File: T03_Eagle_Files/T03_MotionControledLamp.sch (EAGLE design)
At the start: 32 parts, among them U1 ATMEGA328P-MU, U4 TPS61161ADRVT, X2 16MHz

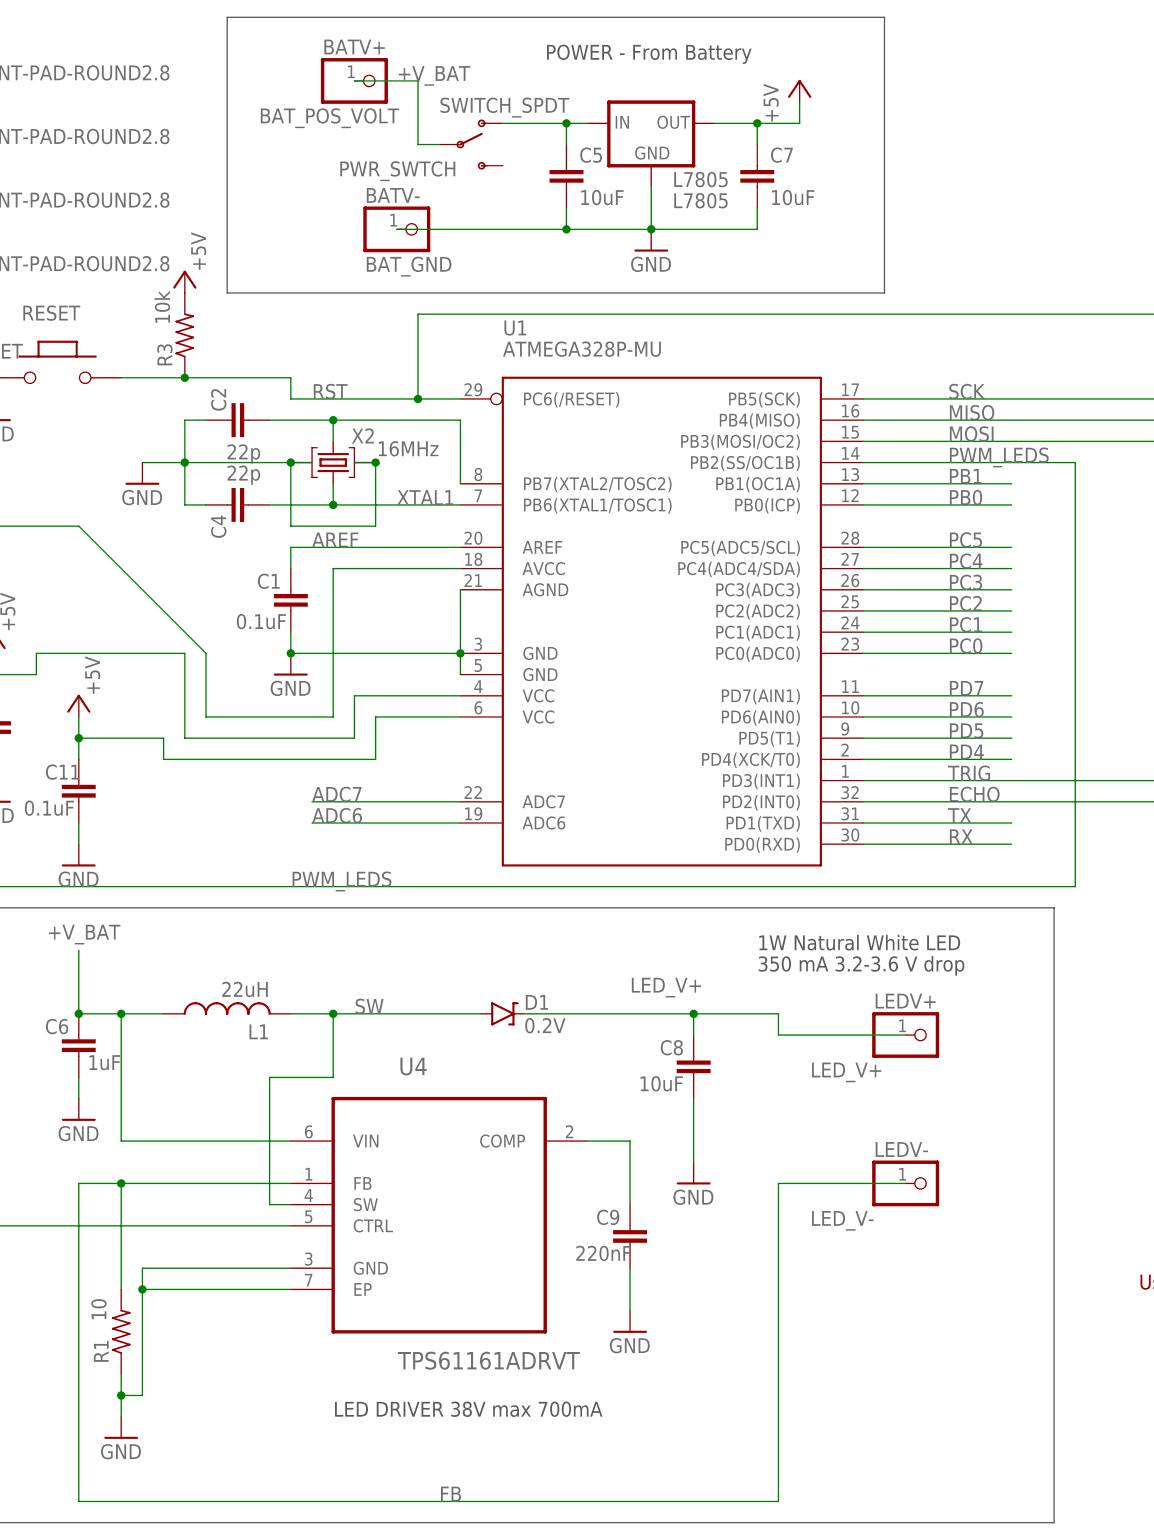
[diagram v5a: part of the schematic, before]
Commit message: Added molex headers to schematic
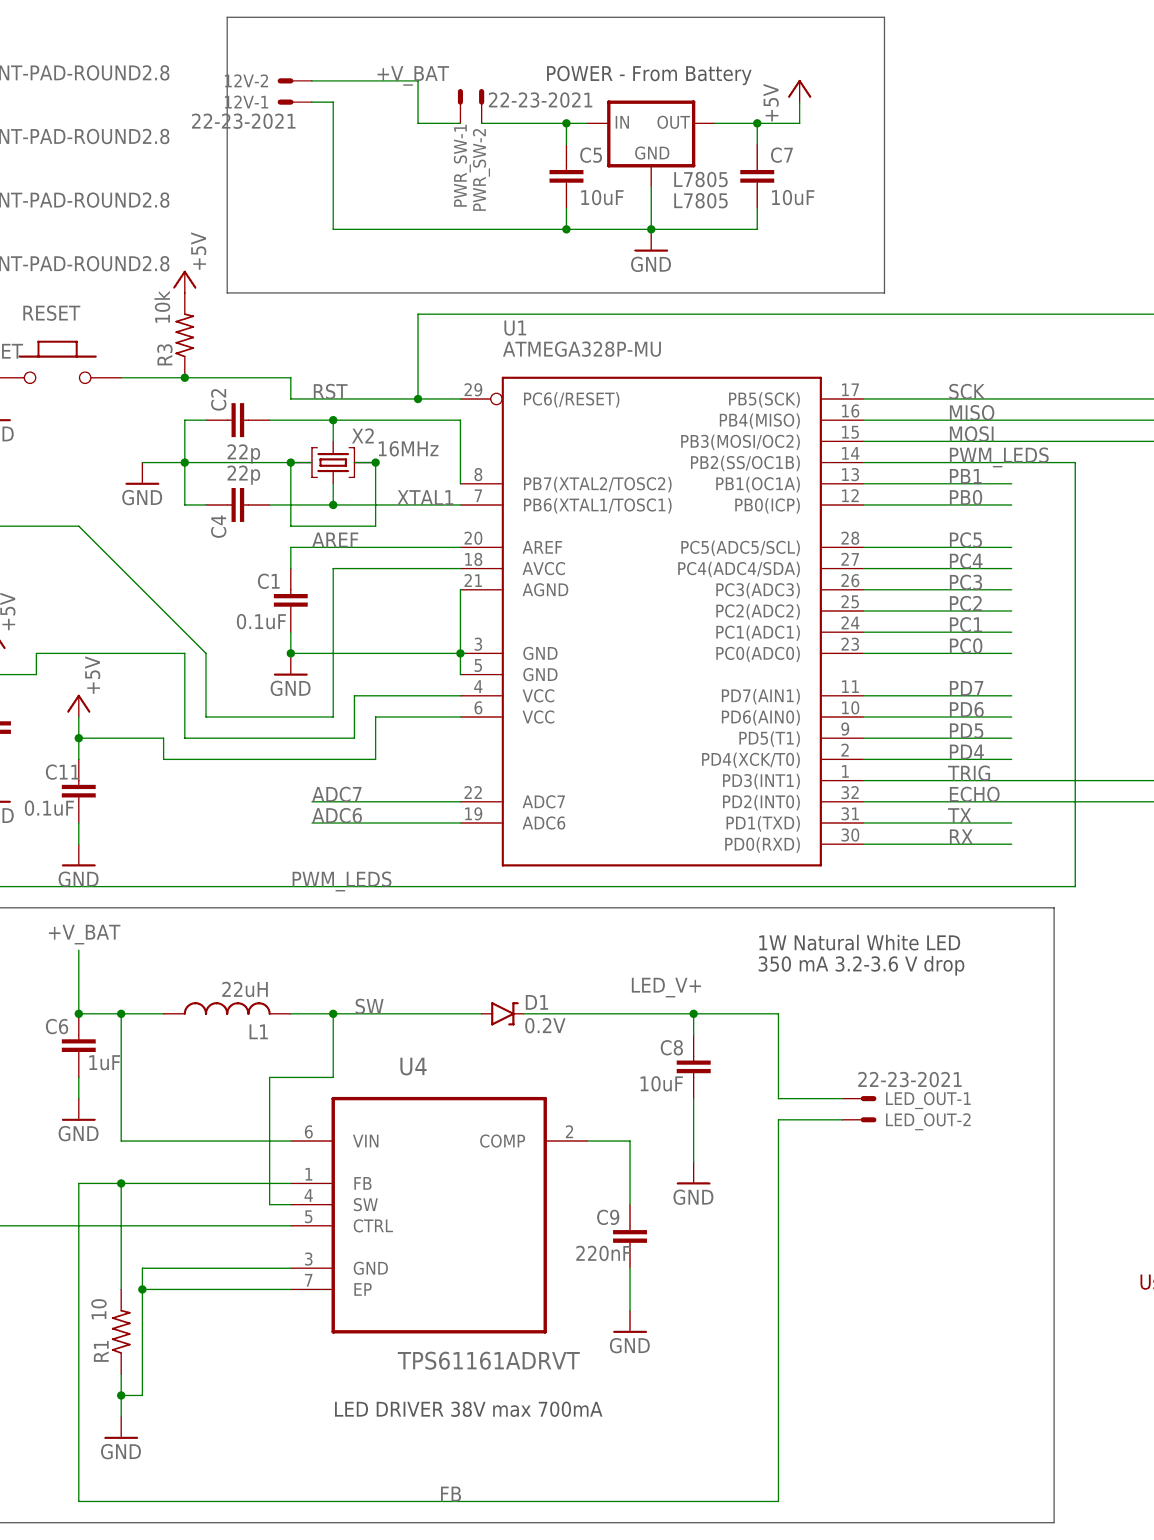
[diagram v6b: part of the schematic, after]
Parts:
- removed BATV+: BAT_POS_VOLT, adafruit:PINHD-1X1
- removed BATV-: BAT_GND, adafruit:PINHD-1X1
- removed LEDV+: LED_V+, adafruit:PINHD-1X1
- removed LEDV-: LED_V-, adafruit:PINHD-1X1
- removed PWR_SWTCH: SWITCH_SPDT, SparkFun-Electromechanical:SWITCH_SPDT
- added 12V, LED_OUT, PWR_SW: 22-23-2021, con-molex:22-23-2021
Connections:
- net +V_BAT: now also 12V-2.S, PWR_SW-1.S; no longer BATV+.1, PWR_SWTCH.P
- net FB: now also LED_OUT-2.S; no longer LEDV-.1
- net GND: now also 12V-1.S; no longer BATV-.1
- net LED_V+: now also LED_OUT-1.S; no longer LEDV+.1
- net N$4: now also PWR_SW-2.S; no longer PWR_SWTCH.O
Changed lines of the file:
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@@
 <part name="C5" library="rcl" deviceset="C-EU" device="C1206" value="10uF"/>
 <part name="C7" library="rcl" deviceset="C-EU" device="C1206" value="10uF"/>
-<part name="PWR_SWTCH" library="SparkFun-Electromechanical" deviceset="SWITCH_SPDT" device=""/>
 <part name="JP1" library="SparkFun-Connectors" deviceset="M05X2" device="SHD_LOCK" value="AVR_SPI_PROG"/>
 <part name="GND6" library="SparkFun-Aesthetics" deviceset="GND" device=""/>
@@
 <part name="GND10" library="supply1" deviceset="GND" device=""/>
 <part name="GND11" library="supply1" deviceset="GND" device=""/>
-<part name="BATV+" library="adafruit" deviceset="PINHD-1X1" device="" value="BAT_POS_VOLT"/>
-<part name="BATV-" library="adafruit" deviceset="PINHD-1X1" device="" value="BAT_GND"/>
 <part name="R3" library="rcl" deviceset="R-US_" device="M1206" value="10k"/>
 <part name="L7805" library="v-reg" deviceset="78XXL" device="" value="L7805"/>
 <part name="SR04" library="con-molex" deviceset="22-23-2041" device=""/>
-<part name="LEDV+" library="adafruit" deviceset="PINHD-1X1" device="" value="LED_V+"/>
-<part name="LEDV-" library="adafruit" deviceset="PINHD-1X1" device="" value="LED_V-"/>
 <part name="P+5" library="supply1" deviceset="+5V" device=""/>
 <part name="H1" library="holes" deviceset="MOUNT-PAD-ROUND" device="2.8"/>
@@
 <part name="P+9" library="supply1" deviceset="+5V" device=""/>
 <part name="GND14" library="SparkFun-Aesthetics" deviceset="GND" device=""/>
+<part name="PWR_SW" library="con-molex" deviceset="22-23-2021" device=""/>
+<part name="12V" library="con-molex" deviceset="22-23-2021" device=""/>
+<part name="LED_OUT" library="con-molex" deviceset="22-23-2021" device=""/>
 </parts>
 <sheets>
@@
 <wire x1="43.18" y1="149.86" x2="121.92" y2="149.86" width="0.1524" layer="97"/>
 <wire x1="121.92" y1="149.86" x2="121.92" y2="182.88" width="0.1524" layer="97"/>
-<text x="81.28" y="177.8" size="1.778" layer="97">POWER - From Battery</text>
+<text x="81.28" y="175.26" size="1.778" layer="97">POWER - From Battery</text>
 <wire x1="167.64" y1="119.38" x2="167.64" y2="68.58" width="0.1524" layer="97"/>
 <wire x1="167.64" y1="68.58" x2="238.76" y2="68.58" width="0.1524" layer="97"/>
@@
 <instance part="C5" gate="G$1" x="83.82" y="165.1"/>
 <instance part="C7" gate="G$1" x="106.68" y="165.1"/>
-<instance part="PWR_SWTCH" gate="G$1" x="71.12" y="167.64" smashed="yes">
-<attribute name="NAME" x="56.515" y="163.83" size="1.778" layer="95"/>
-<attribute name="VALUE" x="68.58" y="171.45" size="1.778" layer="96"/>
-</instance>
 <instance part="JP1" gate="G$1" x="208.28" y="162.56"/>
 <instance part="GND6" gate="1" x="228.6" y="149.86"/>
@@
 <instance part="GND10" gate="1" x="25.4" y="50.8"/>
 <instance part="GND11" gate="1" x="91.44" y="25.4"/>
-<instance part="BATV+" gate="G$1" x="60.96" y="175.26" smashed="yes">
-<attribute name="NAME" x="54.61" y="178.435" size="1.778" layer="95"/>
-<attribute name="VALUE" x="46.99" y="170.18" size="1.778" layer="96"/>
-</instance>
-<instance part="BATV-" gate="G$1" x="66.04" y="157.48" smashed="yes">
-<attribute name="NAME" x="59.69" y="160.655" size="1.778" layer="95"/>
-<attribute name="VALUE" x="59.69" y="152.4" size="1.778" layer="96"/>
-</instance>
 <instance part="R3" gate="G$1" x="38.1" y="144.78" smashed="yes" rot="R90">
 <attribute name="NAME" x="36.6014" y="140.97" size="1.778" layer="95" rot="R90"/>
@@
 <instance part="SR04" gate="-3" x="190.5" y="93.98"/>
 <instance part="SR04" gate="-4" x="190.5" y="91.44"/>
-<instance part="LEDV+" gate="G$1" x="127" y="60.96" smashed="yes">
-<attribute name="NAME" x="120.65" y="64.135" size="1.778" layer="95"/>
-<attribute name="VALUE" x="113.03" y="55.88" size="1.778" layer="96"/>
-</instance>
-<instance part="LEDV-" gate="G$1" x="127" y="43.18" smashed="yes">
-<attribute name="NAME" x="120.65" y="46.355" size="1.778" layer="95"/>
-<attribute name="VALUE" x="113.03" y="38.1" size="1.778" layer="96"/>
-</instance>
 <instance part="P+5" gate="1" x="38.1" y="152.4" smashed="yes">
 <attribute name="VALUE" x="40.64" y="152.4" size="1.778" layer="96" rot="R90"/>
@@
 </instance>
 <instance part="GND14" gate="1" x="228.6" y="91.44"/>
+<instance part="PWR_SW" gate="-1" x="71.12" y="172.72" smashed="yes" rot="R90">
+<attribute name="NAME" x="70.358" y="170.18" size="1.524" layer="95" rot="R270"/>
+<attribute name="VALUE" x="87.122" y="173.863" size="1.778" layer="96" rot="R180"/>
+</instance>
+<instance part="PWR_SW" gate="-2" x="73.66" y="172.72" smashed="yes" rot="R90">
+<attribute name="NAME" x="74.168" y="159.512" size="1.524" layer="95" rot="R90"/>
+</instance>
+<instance part="12V" gate="-1" x="50.8" y="172.72" rot="R180"/>
+<instance part="12V" gate="-2" x="50.8" y="175.26" rot="R180"/>
+<instance part="LED_OUT" gate="-1" x="119.38" y="53.34"/>
+<instance part="LED_OUT" gate="-2" x="119.38" y="50.8"/>
 </instances>
 <busses>
@@
 <wire x1="83.82" y1="157.48" x2="93.98" y2="157.48" width="0.1524" layer="91"/>
 <junction x="83.82" y="157.48"/>
-<pinref part="BATV-" gate="G$1" pin="1"/>
-<wire x1="83.82" y1="157.48" x2="63.5" y2="157.48" width="0.1524" layer="91"/>
+<wire x1="83.82" y1="157.48" x2="55.88" y2="157.48" width="0.1524" layer="91"/>
 <pinref part="L7805" gate="A" pin="GND"/>
+<wire x1="55.88" y1="157.48" x2="55.88" y2="172.72" width="0.1524" layer="91"/>
+<pinref part="12V" gate="-1" pin="S"/>
+<wire x1="55.88" y1="172.72" x2="53.34" y2="172.72" width="0.1524" layer="91"/>
 </segment>
 <segment>
@@
 <pinref part="C5" gate="G$1" pin="1"/>
 <wire x1="83.82" y1="170.18" x2="83.82" y2="167.64" width="0.1524" layer="91"/>
-<pinref part="PWR_SWTCH" gate="G$1" pin="O"/>
-<wire x1="76.2" y1="170.18" x2="83.82" y2="170.18" width="0.1524" layer="91"/>
+<wire x1="73.66" y1="170.18" x2="83.82" y2="170.18" width="0.1524" layer="91"/>
 <junction x="83.82" y="170.18"/>
 <pinref part="L7805" gate="A" pin="IN"/>
+<pinref part="PWR_SW" gate="-2" pin="S"/>
 </segment>
 </net>
@@
 <wire x1="78.74" y1="63.5" x2="99.06" y2="63.5" width="0.1524" layer="91"/>
 <wire x1="99.06" y1="63.5" x2="109.22" y2="63.5" width="0.1524" layer="91"/>
-<wire x1="109.22" y1="63.5" x2="109.22" y2="60.96" width="0.1524" layer="91"/>
 <pinref part="C8" gate="G$1" pin="2"/>
 <wire x1="99.06" y1="63.5" x2="99.06" y2="60.96" width="0.1524" layer="91"/>
 <junction x="99.06" y="63.5"/>
-<pinref part="LEDV+" gate="G$1" pin="1"/>
-<wire x1="124.46" y1="60.96" x2="109.22" y2="60.96" width="0.1524" layer="91"/>
 <label x="91.44" y="66.04" size="1.778" layer="95"/>
+<pinref part="LED_OUT" gate="-1" pin="S"/>
+<wire x1="116.84" y1="53.34" x2="109.22" y2="53.34" width="0.1524" layer="91"/>
+<wire x1="109.22" y1="53.34" x2="109.22" y2="63.5" width="0.1524" layer="91"/>
 </segment>
 </net>
@@
 <wire x1="30.48" y1="43.18" x2="30.48" y2="30.48" width="0.1524" layer="91"/>
 <junction x="30.48" y="43.18"/>
-<pinref part="LEDV-" gate="G$1" pin="1"/>
-<wire x1="124.46" y1="43.18" x2="109.22" y2="43.18" width="0.1524" layer="91"/>
-<wire x1="109.22" y1="43.18" x2="109.22" y2="5.08" width="0.1524" layer="91"/>
+<wire x1="109.22" y1="50.8" x2="109.22" y2="5.08" width="0.1524" layer="91"/>
 <wire x1="109.22" y1="5.08" x2="25.4" y2="5.08" width="0.1524" layer="91"/>
 <label x="68.58" y="5.08" size="1.778" layer="95"/>
+<pinref part="LED_OUT" gate="-2" pin="S"/>
+<wire x1="109.22" y1="50.8" x2="116.84" y2="50.8" width="0.1524" layer="91"/>
 </segment>
 </net>
@@
 <net name="+V_BAT" class="0">
 <segment>
-<wire x1="66.04" y1="175.26" x2="66.04" y2="167.64" width="0.1524" layer="91"/>
-<pinref part="PWR_SWTCH" gate="G$1" pin="P"/>
-<wire x1="66.04" y1="167.64" x2="68.58" y2="167.64" width="0.1524" layer="91"/>
-<pinref part="BATV+" gate="G$1" pin="1"/>
-<wire x1="66.04" y1="175.26" x2="58.42" y2="175.26" width="0.1524" layer="91"/>
-<label x="63.5" y="175.26" size="1.778" layer="95"/>
-</segment>
-<segment>
+<wire x1="66.04" y1="175.26" x2="66.04" y2="170.18" width="0.1524" layer="91"/>
+<label x="60.96" y="175.26" size="1.778" layer="95"/>
+<wire x1="66.04" y1="175.26" x2="53.34" y2="175.26" width="0.1524" layer="91"/>
+<pinref part="12V" gate="-2" pin="S"/>
+<pinref part="PWR_SW" gate="-1" pin="S"/>
+<wire x1="71.12" y1="170.18" x2="66.04" y2="170.18" width="0.1524" layer="91"/>
+</segment>
+<segment>
